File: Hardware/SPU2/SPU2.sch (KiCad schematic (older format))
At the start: 736 parts, among them J1 Conn_Coaxial, J2 Conn_02x13_Counter_Clockwise, J3 Conn_01x02, J4 Conn_01x04_Male, Q2 BC547, Q3 BC547, Q4 BC547, SW1 SW_Push, SW2 SW_SPDT, SW3 SW_DIP_x02, U1 74LS86, U10 74LS08, U11 74LS173, U12 74LS173, U13 74LS161, U14 74LS161, U15 74LS161, U16 74LS173, U17 74LS173, U18 NE555, U19 74LS173, U2 74LS86, U20 74LS173, U21 74LS173, U22 74LS173, U23 74LS173, U24 74LS173, U25 74LS245, U26 M84Z02, U27 M84Z02, U28 74LS245, U29 74LS00, U3 74LS245, U30 28c64, U31 28c64, U32 74LS245, U33 74LS245, U34 74LS245, U35 74LS245, U36 74LS245, U37 74LS08, U38 74HCT574, U39 74HCT574, U4 74LS283, U40 74LS161, U41 74LS04, U42 74LS08, U43 NE555, U44 NE555, U45 74HCT574, U46 74HCT574, U47 74HCT574, U48 74HCT574, U49 74HCT574, U5 74LS283, U50 74HCT574, U51 74HCT574, U52 74HCT574, U53 74HCT574, U54 74HCT574, U55 74HCT574, U56 74HCT574, U57 74HCT574, U58 74HCT574, U59 74HCT574, U6 4077, U60 74HCT574, U61 INTEL2716, U62 74LS08, U63 INTEL2716, U64 74LS08, U65 74LS08, U66 74LS08, U67 74LS08, U68 INTEL2716, U69 CD4514B, U7 4077, U70 74LS157, U76 74LS157, U77 74LS157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

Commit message: done stuff
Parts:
- gave numbers to parts that had none: 10
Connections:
- net GND: no longer D122.1 (K), D123.1 (K), D124.1 (K), D125.1 (K), D126.1 (K), D127.1 (K), D128.1 (K), D129.1 (K)
- net RAMOBUS0: now also U70.2 (I0a); no longer U70.3 (I1a)
- net RAMOBUS1: now also U70.5 (I0b); no longer U70.6 (I1b)
- net RAMOBUS10: now also U77.11 (I0c); no longer U77.10 (I1c)
- net RAMOBUS11: now also U77.14 (I0d); no longer U77.13 (I1d)
- net RAMOBUS12: now also U78.2 (I0a); no longer U78.3 (I1a)
- net RAMOBUS13: now also U78.5 (I0b); no longer U78.6 (I1b)
- net RAMOBUS14: now also U78.11 (I0c); no longer U78.10 (I1c)
- net RAMOBUS15: now also U78.14 (I0d); no longer U78.13 (I1d)
- net RAMOBUS2: now also U70.11 (I0c); no longer U70.10 (I1c)
- net RAMOBUS3: now also U70.14 (I0d); no longer U70.13 (I1d)
- net RAMOBUS4: now also U76.2 (I0a); no longer U76.3 (I1a)
- net RAMOBUS5: now also U76.5 (I0b); no longer U76.6 (I1b)
- net RAMOBUS6: now also U76.11 (I0c); no longer U76.10 (I1c)
- net RAMOBUS7: now also U76.14 (I0d); no longer U76.13 (I1d)
- net RAMOBUS8: now also U77.2 (I0a); no longer U77.3 (I1a)
- net RAMOBUS9: now also U77.5 (I0b); no longer U77.6 (I1b)
- net ROM0: now also U70.3 (I1a); no longer U70.2 (I0a)
- net ROM1: now also U70.6 (I1b); no longer U70.5 (I0b)
- net ROM10: now also U77.10 (I1c); no longer U77.11 (I0c)
- net ROM11: now also U77.13 (I1d); no longer U77.14 (I0d)
- net ROM12: now also U78.3 (I1a); no longer U78.2 (I0a)
- net ROM13: now also U78.6 (I1b); no longer U78.5 (I0b)
- net ROM14: now also U78.10 (I1c); no longer U78.11 (I0c)
- net ROM15: now also U78.13 (I1d); no longer U78.14 (I0d)
- net ROM2: now also U70.10 (I1c); no longer U70.11 (I0c)
- net ROM3: now also U70.13 (I1d); no longer U70.14 (I0d)
- net ROM4: now also U76.3 (I1a); no longer U76.2 (I0a)
- net ROM5: now also U76.6 (I1b); no longer U76.5 (I0b)
- net ROM6: now also U76.10 (I1c); no longer U76.11 (I0c)
- net ROM7: now also U76.13 (I1d); no longer U76.14 (I0d)
- net ROM8: now also U77.3 (I1a); no longer U77.2 (I0a)
- net ROM9: now also U77.6 (I1b); no longer U77.5 (I0b)
- net NE555_CLK: now reaches R125.2, U41.8
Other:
- note added: "RAM (LEDs)\n"
- note added: "excess NAND gates (RAM)\n"
- note removed: "architecture diagram\n\n"
- note removed: "ram leds"
- note removed: "übrige nand gates (für ram)"
- moved on the sheet: C1, C10, C11, C12, C13, C14, C15, C16, C17, C18, C19, C22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

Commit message: existance is pain
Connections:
- net ADDR0: no longer U30.10 (A0), U31.10 (A0)
- net ADDR1: no longer U30.9 (A1), U31.9 (A1)
- net ADDR10: no longer U30.21 (A10), U31.21 (A10)
- net ADDR2: no longer U30.8 (A2), U31.8 (A2)
- net ADDR3: no longer U30.7 (A3), U31.7 (A3)
- net ADDR4: no longer U30.6 (A4), U31.6 (A4)
- net ADDR5: no longer U30.5 (A5), U31.5 (A5)
- net ADDR6: no longer U30.4 (A6), U31.4 (A6)
- net ADDR7: no longer U30.3 (A7), U31.3 (A7)
- net ADDR8: no longer U30.25 (A8), U31.25 (A8)
- net ADDR9: no longer U30.24 (A9), U31.24 (A9)
- net MEMADDR0: now also U30.10 (A0), U31.10 (A0)
- net MEMADDR1: now also U30.9 (A1), U31.9 (A1)
- net MEMADDR10: now also U30.21 (A10), U31.21 (A10)
- net MEMADDR2: now also U30.8 (A2), U31.8 (A2)
- net MEMADDR3: now also U30.7 (A3), U31.7 (A3)
- net MEMADDR4: now also U30.6 (A4), U31.6 (A4)
- net MEMADDR5: now also U30.5 (A5), U31.5 (A5)
- net MEMADDR6: now also U30.4 (A6), U31.4 (A6)
- net MEMADDR7: now also U30.3 (A7), U31.3 (A7)
- net MEMADDR8: now also U30.25 (A8), U31.25 (A8)
- net MEMADDR9: now also U30.24 (A9), U31.24 (A9)
- no-connect marks 41 -> 39
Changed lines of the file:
@@
 	1    0    0    -1
 $EndComp
-NoConn ~ 15450 5950
-NoConn ~ 14650 3200
 $Comp
 L Device:C C84
@@
 Wire Wire Line
 	16650 8200 16650 6250
-Connection ~ 16650 6250
 Wire Wire Line
 	16600 8300 16600 6350
 Connection ~ 16600 6350
-Text GLabel 16050 5000 2    50   BiDi ~ 0
-ADDR
-Text Label 16250 5350 0    50   ~ 0
-ADDR10
-Text Label 16250 5450 0    50   ~ 0
-ADDR9
-Text Label 16250 5550 0    50   ~ 0
-ADDR8
-Entry Wire Line
-	16150 5350 16050 5250
-Entry Wire Line
-	16150 5450 16050 5350
-Entry Wire Line
-	16150 5550 16050 5450
-Text Label 16250 5650 0    50   ~ 0
-ADDR7
-Text Label 16250 5750 0    50   ~ 0
-ADDR6
-Text Label 16250 5850 0    50   ~ 0
-ADDR5
-Text Label 16250 5950 0    50   ~ 0
-ADDR4
-Entry Wire Line
-	16150 5650 16050 5550
-Entry Wire Line
-	16150 5750 16050 5650
-Entry Wire Line
-	16150 5850 16050 5750
-Entry Wire Line
-	16150 5950 16050 5850
-Entry Wire Line
-	16150 6350 16050 6250
-Entry Wire Line
-	16150 6250 16050 6150
-Entry Wire Line
-	16150 6150 16050 6050
-Entry Wire Line
-	16150 6050 16050 5950
-Text Label 16250 6350 0    50   ~ 0
-ADDR0
-Text Label 16250 6250 0    50   ~ 0
-ADDR1
-Text Label 16250 6150 0    50   ~ 0
-ADDR2
-Text Label 16250 6050 0    50   ~ 0
-ADDR3
 Wire Wire Line
 	16150 6350 16600 6350
 Wire Wire Line
-	16150 6250 16650 6250
-Wire Wire Line
 	16150 6150 16700 6150
 Wire Wire Line
@@
 EndData
 $EndBitmap
+Entry Wire Line
+	16150 5350 16050 5250
+Entry Wire Line
+	16150 5450 16050 5350
+Entry Wire Line
+	16150 5550 16050 5450
+Entry Wire Line
+	16150 5650 16050 5550
+Entry Wire Line
+	16150 5750 16050 5650
+Entry Wire Line
+	16150 5850 16050 5750
+Entry Wire Line
+	16150 5950 16050 5850
+Entry Wire Line
+	16150 6350 16050 6250
+Entry Wire Line
+	16150 6250 16050 6150
+Entry Wire Line
+	16150 6150 16050 6050
+Entry Wire Line
+	16150 6050 16050 5950
+Text GLabel 16050 5000 1    50   BiDi ~ 0
+MEMADDR
+Text Label 16500 6350 2    50   ~ 0
+MEMADDR0
+Text Label 16500 6250 2    50   ~ 0
+MEMADDR1
+Text Label 16500 6150 2    50   ~ 0
+MEMADDR2
+Text Label 16500 6050 2    50   ~ 0
+MEMADDR3
+Text Label 16500 5950 2    50   ~ 0
+MEMADDR4
+Text Label 16500 5850 2    50   ~ 0
+MEMADDR5
+Text Label 16500 5750 2    50   ~ 0
+MEMADDR6
+Text Label 16500 5650 2    50   ~ 0
+MEMADDR7
+Text Label 16500 5550 2    50   ~ 0
+MEMADDR8
+Text Label 16500 5450 2    50   ~ 0
+MEMADDR9
+Text Label 16500 5350 2    50   ~ 0
+MEMADDR10
+Wire Wire Line
+	16150 6250 16650 6250
 Wire Bus Line
 	29950 14350 29950 14550
@@
 	4050 4750 4050 5650
 Wire Bus Line
-	16050 5000 16050 6250
-Wire Bus Line
 	12300 10350 12300 11800
 Wire Bus Line
@@
 	21950 6250 21950 7250
 Wire Bus Line
+	16050 5000 16050 6250
+Wire Bus Line
 	22500 13550 22500 21900
 Wire Bus Line
@@
 Wire Bus Line
 	13500 6000 15150 6000
+Connection ~ 16650 6250
 $EndSCHEMATC

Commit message: done stuff
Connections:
- net GND: now also D122.1 (K), D123.1 (K), D124.1 (K), D125.1 (K), D126.1 (K), D127.1 (K), D128.1 (K), D129.1 (K), D178.1 (K), D179.1 (K), D180.1 (K), D181.1 (K), D183.1 (K), D185.1 (K), D187.1 (K), D189.1 (K), U36.6 (A4), U36.7 (A5), U36.8 (A6), U36.9 (A7)
- net MEM12: no longer U36.6 (A4)
- net MEM13: no longer U36.7 (A5)
- net MEM14: no longer U36.8 (A6)
- net MEM15: no longer U36.9 (A7)
- no-connect marks 39 -> 43
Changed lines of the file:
@@
 Wire Wire Line
 	24650 5500 23100 5500
-Wire Wire Line
-	23000 5600 24650 5600
-Wire Wire Line
-	24650 5700 22900 5700
-Wire Wire Line
-	22800 5800 24650 5800
-Wire Wire Line
-	24650 5900 22700 5900
 NoConn ~ 25650 5900
 NoConn ~ 25650 5800
@@
 L power:GND #PWR0288
 U 1 1 762D8970
-P 12350 15950
-F 0 "#PWR0288" H 12350 15700 50  0001 C CNN
-F 1 "GND" H 12355 15777 50  0000 C CNN
-F 2 "" H 12350 15950 50  0001 C CNN
-F 3 "" H 12350 15950 50  0001 C CNN
-	1    12350 15950
+P 12500 15950
+F 0 "#PWR0288" H 12500 15700 50  0001 C CNN
+F 1 "GND" H 12505 15777 50  0000 C CNN
+F 2 "" H 12500 15950 50  0001 C CNN
+F 3 "" H 12500 15950 50  0001 C CNN
+	1    12500 15950
 	0    1    1    0
 $EndComp
@@
 Text Label 30750 1700 2    50   ~ 0
 RAMOBUS7
-Text Label 30800 1800 2    50   ~ 0
+Text Label 30750 1800 2    50   ~ 0
 RAMOBUS8
-Text Label 30800 1900 2    50   ~ 0
+Text Label 30750 1900 2    50   ~ 0
 RAMOBUS9
 Text Label 30800 2000 2    50   ~ 0
@@
 	19400 20200 19400 22900
 Wire Wire Line
-	7150 19100 7950 19100
+	7150 19000 7250 19000
 Wire Notes Line
 	12200 12700 12200 8950
@@
 Wire Wire Line
 	16150 6250 16650 6250
+Connection ~ 16650 6250
+Connection ~ 7250 19000
+Wire Wire Line
+	7250 19000 7350 19000
+Connection ~ 7350 19000
+Wire Wire Line
+	7350 19000 7450 19000
+Connection ~ 7450 19000
+Wire Wire Line
+	7450 19000 7550 19000
+Connection ~ 7550 19000
+Wire Wire Line
+	7550 19000 7650 19000
+Connection ~ 7650 19000
+Wire Wire Line
+	7650 19000 7750 19000
+Connection ~ 7750 19000
+Wire Wire Line
+	7750 19000 7850 19000
+Connection ~ 7850 19000
+Wire Wire Line
+	7850 19000 7950 19000
+NoConn ~ 22700 5900
+NoConn ~ 23000 5600
+NoConn ~ 22900 5700
+NoConn ~ 22800 5800
+Wire Wire Line
+	24650 5600 24650 5700
+Connection ~ 24650 5700
+Wire Wire Line
+	24650 5700 24650 5800
+Connection ~ 24650 5800
+Wire Wire Line
+	24650 5800 24650 5900
+Wire Wire Line
+	24650 5800 24500 5800
+Wire Wire Line
+	24500 5800 24500 5850
 Wire Bus Line
 	29950 14350 29950 14550
@@
 	17650 1150 18350 1150
 Wire Bus Line
+	16050 5000 16050 6250
+Wire Bus Line
 	30900 10850 31700 10850
 Wire Bus Line
@@
 	21950 6250 21950 7250
 Wire Bus Line
-	16050 5000 16050 6250
-Wire Bus Line
 	22500 13550 22500 21900
 Wire Bus Line
@@
 Wire Bus Line
 	13500 6000 15150 6000
-Connection ~ 16650 6250
+$Comp
+L power:GND #PWR?
+U 1 1 67DA35BB
+P 24500 5850
+F 0 "#PWR?" H 24500 5600 50  0001 C CNN
+F 1 "GND" H 24505 5677 50  0000 C CNN
+F 2 "" H 24500 5850 50  0001 C CNN
+F 3 "" H 24500 5850 50  0001 C CNN
+	1    24500 5850
+	1    0    0    -1
+$EndComp
+Connection ~ 24500 5800
 $EndSCHEMATC

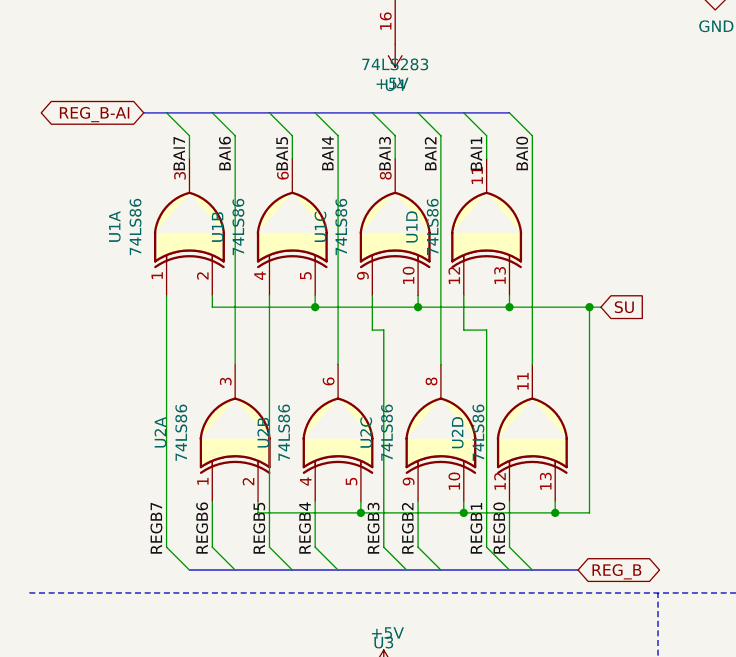
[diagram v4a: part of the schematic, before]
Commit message: added subtraction to Reg B
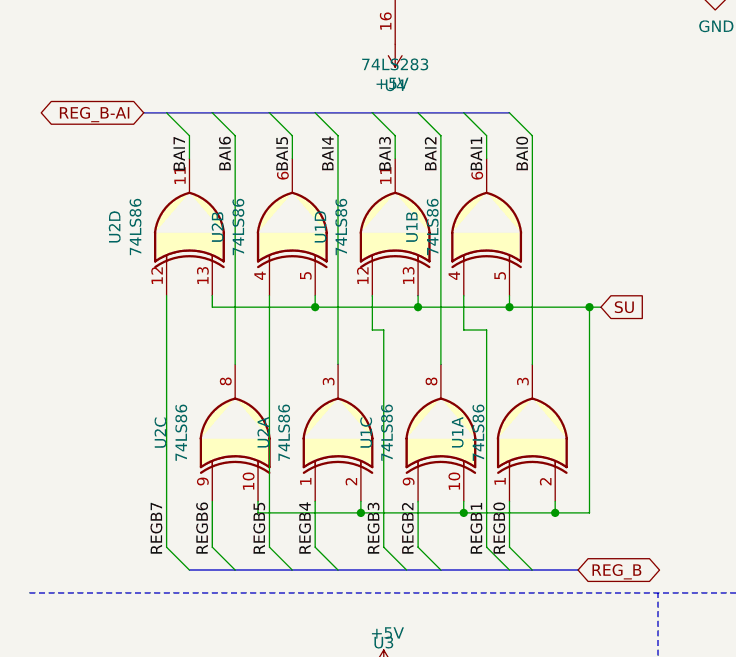
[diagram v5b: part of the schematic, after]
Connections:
- net BAI0: now also U1.3; no longer U2.11
- net BAI1: now also U1.6; no longer U1.11
- net BAI2: now also U1.8; no longer U2.8
- net BAI3: now also U1.11; no longer U1.8
- net BAI4: now also U2.3; no longer U2.6
- net BAI5: now also U2.6; no longer U1.6
- net BAI6: now also U2.8; no longer U2.3
- net BAI7: now also U2.11; no longer U1.3
- net REGB0: now also U1.1; no longer U2.12
- net REGB1: now also U1.4; no longer U1.12
- net REGB2: now also U1.9; no longer U2.9
- net REGB3: now also U1.12; no longer U1.9
- net REGB4: now also U2.1; no longer U2.4
- net REGB5: now also U2.4; no longer U1.4
- net REGB6: now also U2.9; no longer U2.1
- net REGB7: now also U2.12; no longer U1.1
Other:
- moved on the sheet: U1A, U1B, U1C, U1D, U2A, U2B, U2C, U2D
